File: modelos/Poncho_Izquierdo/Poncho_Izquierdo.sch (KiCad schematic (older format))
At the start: 5 parts, among them P1 CONN_5, P2 CONN_4

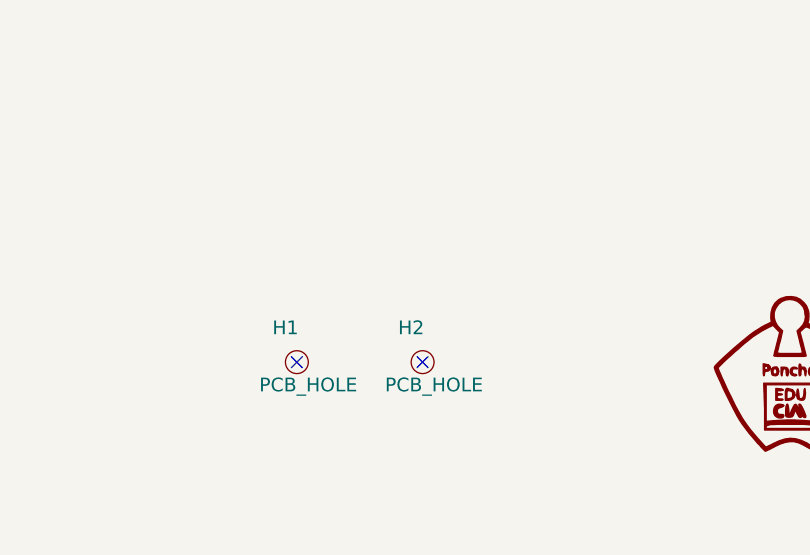
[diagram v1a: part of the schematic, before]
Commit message: * Unifico rótulos en los modelos.
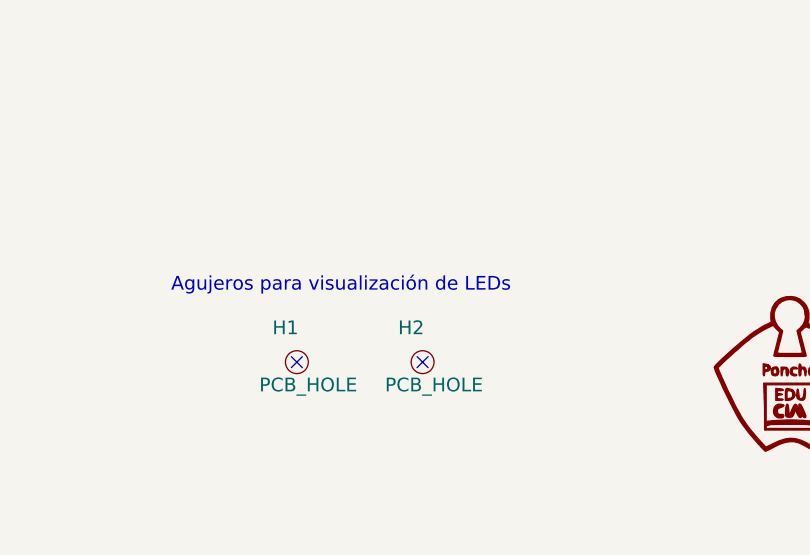
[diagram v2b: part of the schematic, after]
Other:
- note added: "Agujeros para visualización de LEDs"
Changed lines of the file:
@@
 NoConn ~ 8000 5950
 NoConn ~ 8550 5950
+Text Notes 7450 5650 0    60   ~ 0
+Agujeros para visualización de LEDs
 $EndSCHEMATC
